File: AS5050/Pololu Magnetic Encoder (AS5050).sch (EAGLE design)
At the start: 9 parts, among them U1 AS5035

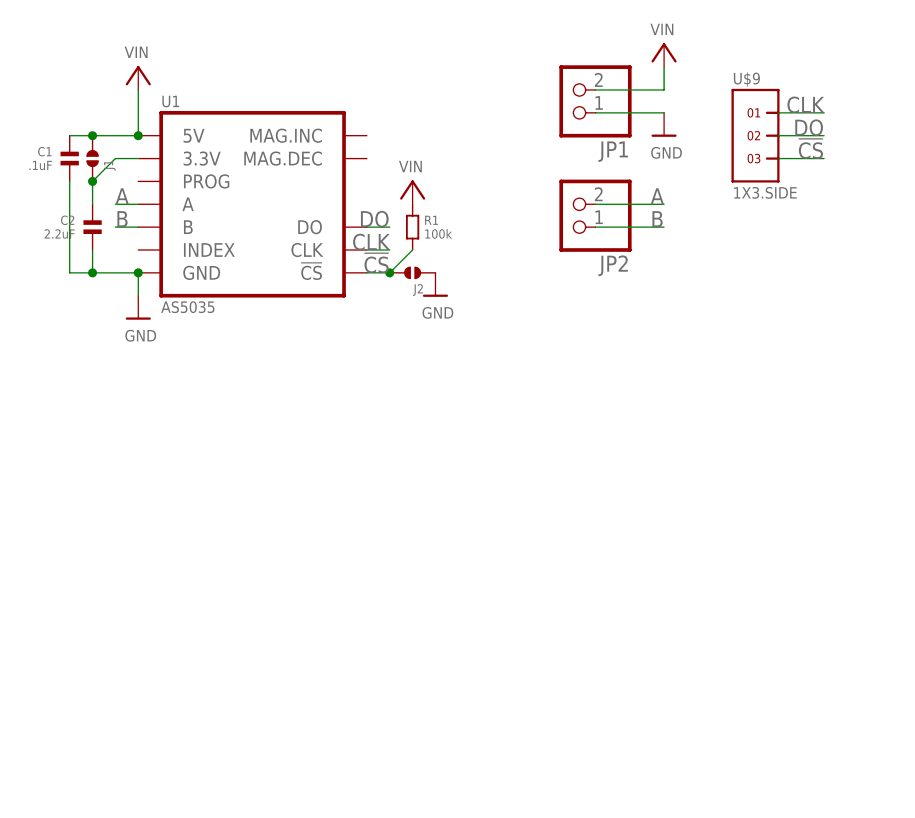
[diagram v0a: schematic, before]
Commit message: Created and completed AS5050 Encoder PCB
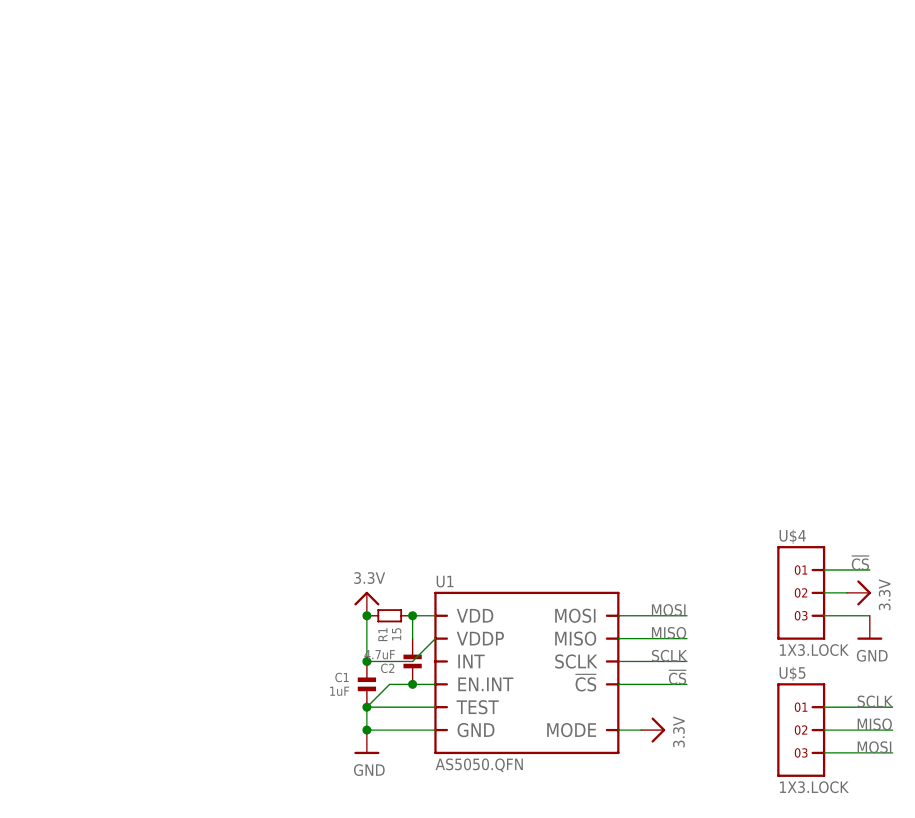
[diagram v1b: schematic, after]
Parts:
- removed J1, J2: (no value), .solderjumper:SOLDERJUMPER.2.LRG.PASTE
- removed JP1, JP2: (no value), microbuilder:HEADER-1X2ROUND
- removed U$9: 1X3.SIDE, .standardheaders:1X3.SIDE
- added U$4, U$5: 1X3.LOCK, headers(.1in):1X3.LOCK
- C1: value .1uF -> 1uF; device .standardparts:CAPACITOR.0603 -> standardparts:CAPACITOR.0603
- C2: value 2.2uF -> 4.7uF; device .standardparts:CAPACITOR.0603 -> standardparts:CAPACITOR.0603
- R1: value 100k -> 15; device .standardparts:RESISTOR.0603 -> standardparts:RESISTOR.0603
- U1: value AS5035 -> AS5050.QFN; device austriamicrosystems:AS5035 -> austriamicrosystems:AS5050.QFN
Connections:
- removed net A: JP2.2, U1.A
- removed net B: JP2.1, U1.B
- removed net CLK: U$9.1, U1.CLK
- removed net DO: U$9.2, U1.DO
- removed net N$4: C2.1, J1.1, U1.3.3V
- removed net VIN: C1.1, J1.2, JP1.2, R1.1, U1.5V
- new net 3.3V: C1.1, R1.1, U$4.2, U1.MODE, U1.VDDP
- new net MISO: U$5.2, U1.MISO
- new net MOSI: U$5.3, U1.MOSI
- new net N$1: C2.2, R1.2, U1.VDD
- new net SCLK: U$5.1, U1.SCLK
- net !CS: now also U$4.1; no longer J2.2, R1.2, U$9.3
- net GND: now also C2.1, U$4.3, U1.EN.INT, U1.TEST; no longer C2.2, J2.1, JP1.1
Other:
- moved on the sheet: C1, C2, R1
